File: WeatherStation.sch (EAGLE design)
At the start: 17 parts, among them J1 EDISON_CONNECTOR_FULLMOUNTING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, J2 EDISON_CONNECTOR_FULLHEADER, U1 MCP73831

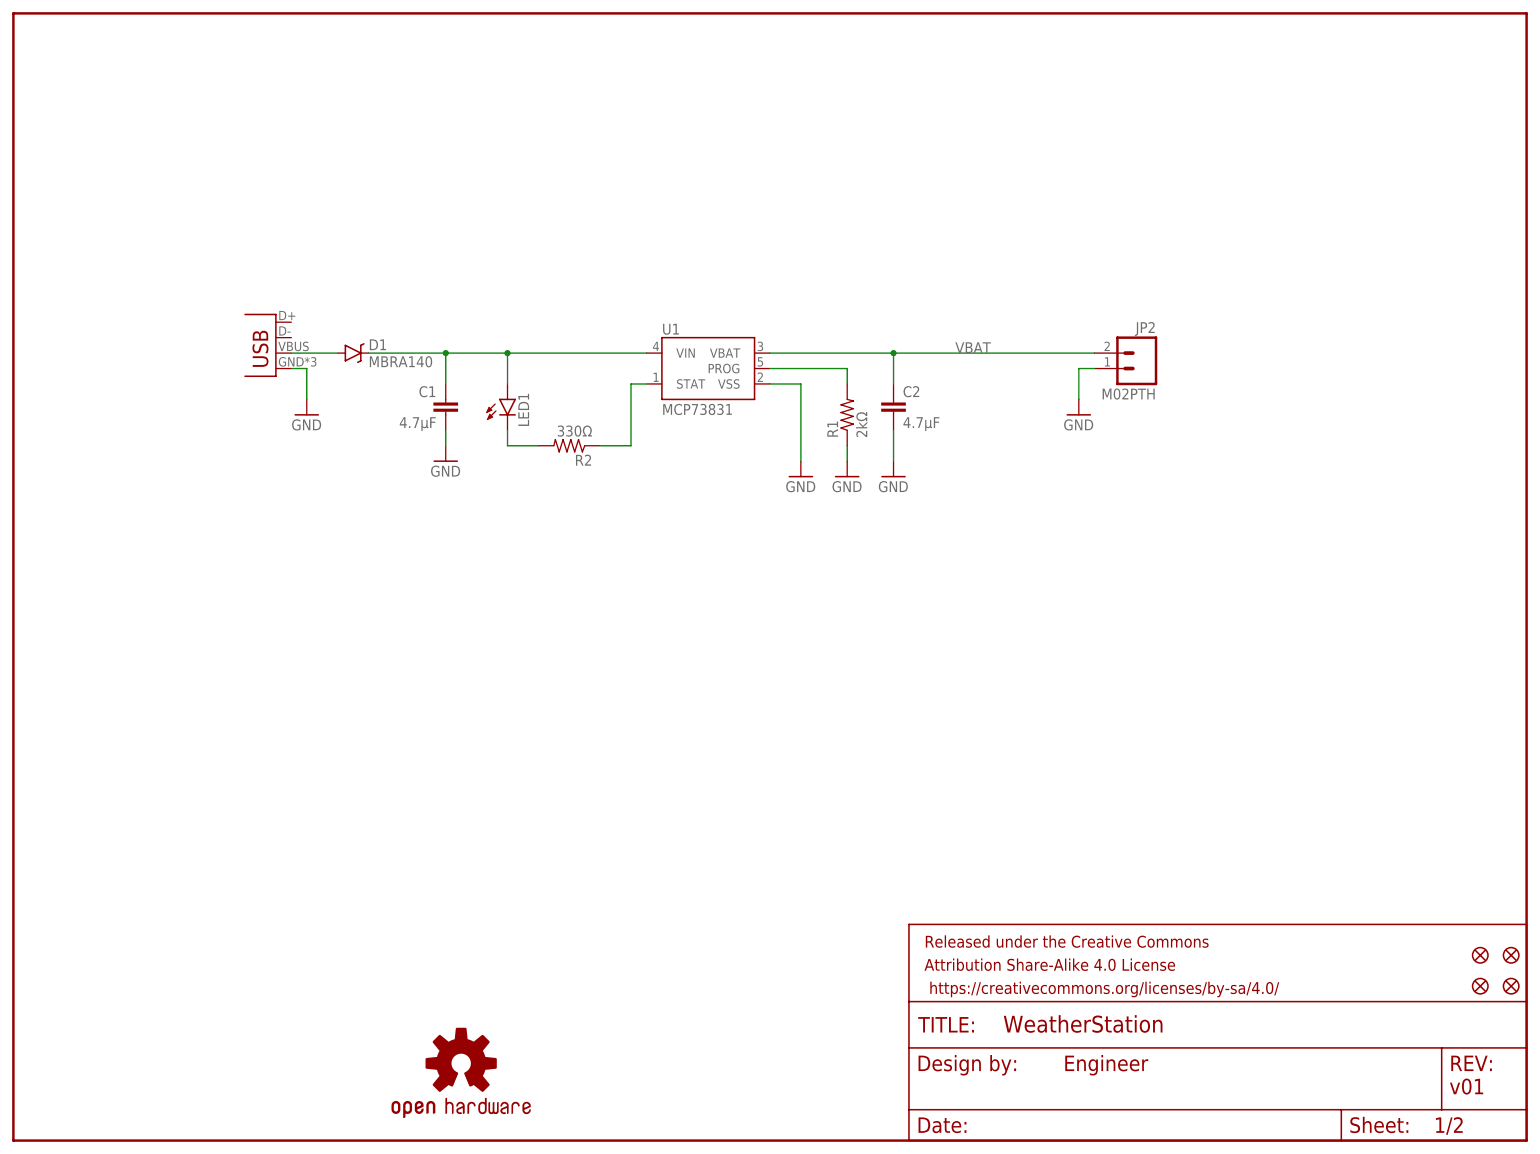
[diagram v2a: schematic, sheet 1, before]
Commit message: placed HTU21D, MPL3115A2, MIC5205-3.3V, PCA9306
RH/temp, barometric pressure/temp, LDO voltage regulator and 1.8-3.3V
logic level shifter.
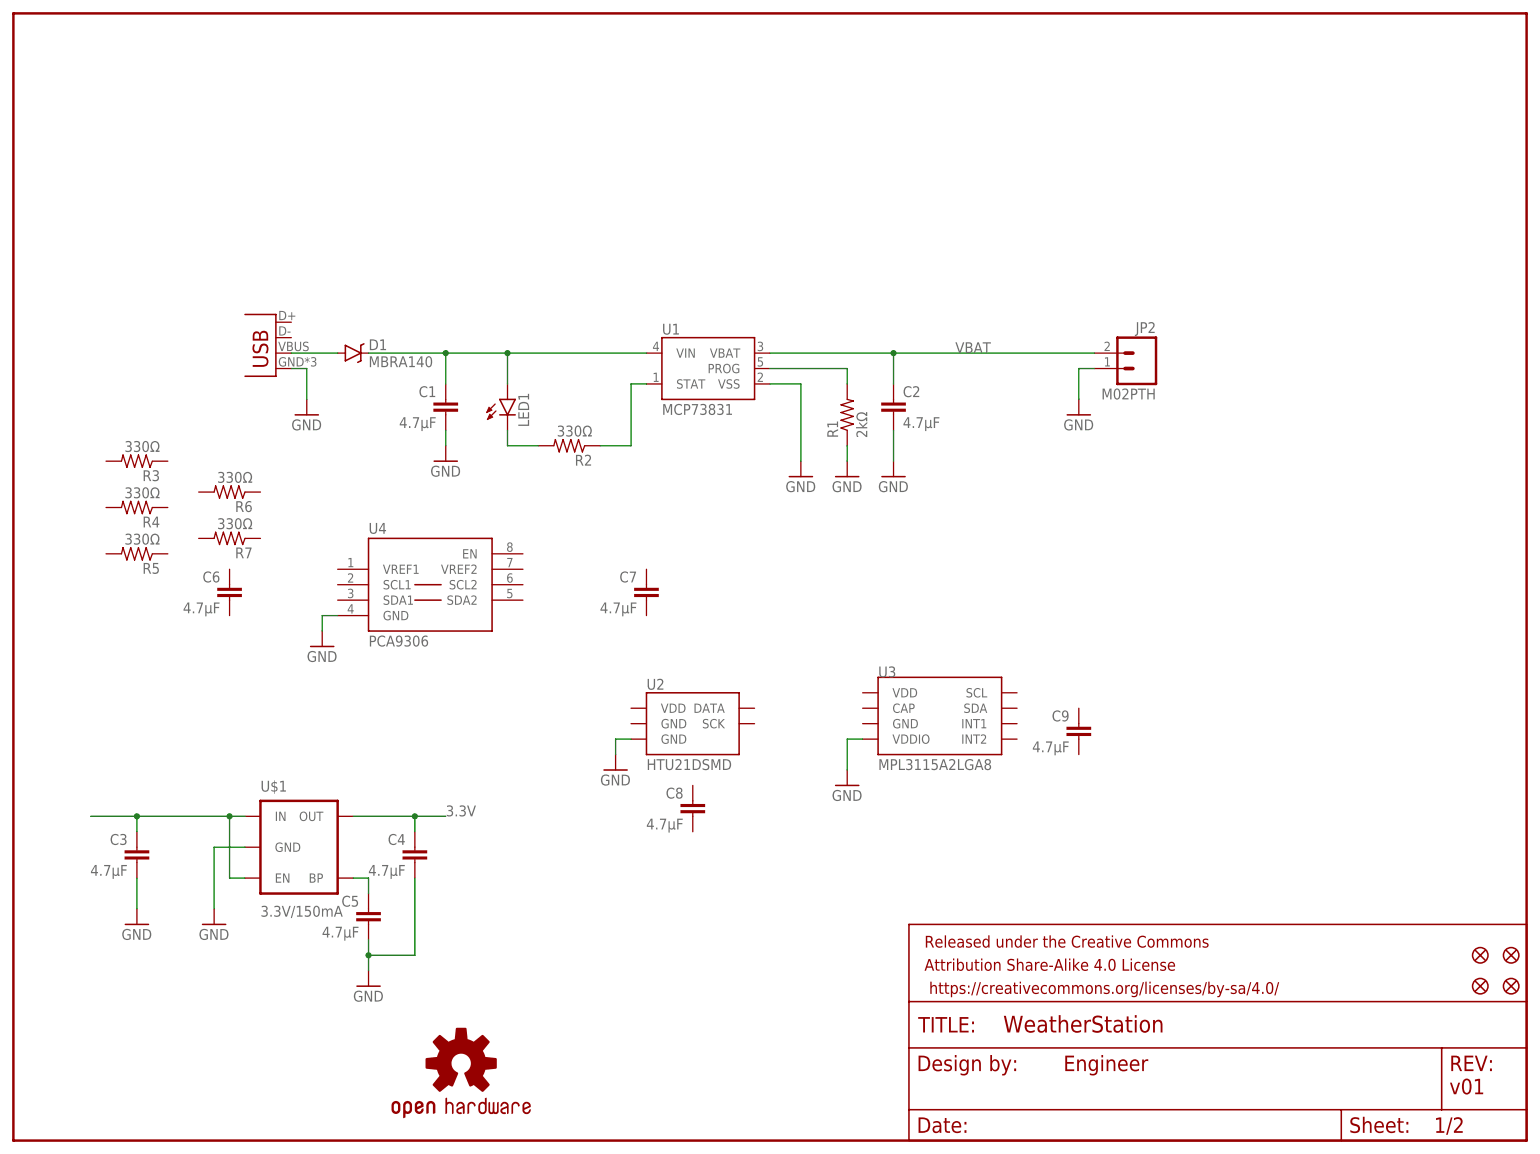
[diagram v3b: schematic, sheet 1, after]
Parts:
- added C3, C4, C5, C6, C7, C8, C9: 4.7µF, SparkFun-Capacitors:CAP0805
- added R3, R4, R5, R6, R7: 330Ω, SparkFun-Resistors:RESISTOR0603-RES
- added U$1: 3.3V/150mA, SparkFun-PowerIC:V_REG_MIC52053.3V
- added U2: HTU21DSMD, SparkFun-Sensors:HTU21DSMD
- added U3: MPL3115A2LGA8, SparkFun-Sensors:MPL3115A2LGA8
- added U4: PCA9306, SparkFun-DigitalIC:PCA9306
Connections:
- new net N$7: C3.1, U$1.EN, U$1.IN
- new net N$8: C5.1, U$1.BP
- net 3.3V: now also C4.1, U$1.OUT
- net GND: now also C3.2, C4.2, C5.2, U$1.GND, U2.GND@7, U3.VDDIO, U4.GND
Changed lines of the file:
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@@
 <part name="JP2" library="SparkFun-Connectors" deviceset="M02" device="PTH"/>
 <part name="GND8" library="SparkFun-Aesthetics" deviceset="GND" device=""/>
+<part name="U2" library="SparkFun-Sensors" deviceset="HTU21D" device="SMD"/>
+<part name="U3" library="SparkFun-Sensors" deviceset="MPL3115A2" device="LGA8"/>
+<part name="U4" library="SparkFun-DigitalIC" deviceset="PCA9306" device="" value="PCA9306"/>
+<part name="U$1" library="SparkFun-PowerIC" deviceset="V_REG_MIC5205" device="3.3V" value="3.3V/150mA"/>
+<part name="GND9" library="SparkFun-Aesthetics" deviceset="GND" device=""/>
+<part name="GND10" library="SparkFun-Aesthetics" deviceset="GND" device=""/>
+<part name="GND11" library="SparkFun-Aesthetics" deviceset="GND" device=""/>
+<part name="GND12" library="SparkFun-Aesthetics" deviceset="GND" device=""/>
+<part name="C3" library="SparkFun-Capacitors" deviceset="CAP" device="0805" value="4.7µF"/>
+<part name="C4" library="SparkFun-Capacitors" deviceset="CAP" device="0805" value="4.7µF"/>
+<part name="C5" library="SparkFun-Capacitors" deviceset="CAP" device="0805" value="4.7µF"/>
+<part name="GND13" library="SparkFun-Aesthetics" deviceset="GND" device=""/>
+<part name="GND14" library="SparkFun-Aesthetics" deviceset="GND" device=""/>
+<part name="C6" library="SparkFun-Capacitors" deviceset="CAP" device="0805" value="4.7µF"/>
+<part name="C7" library="SparkFun-Capacitors" deviceset="CAP" device="0805" value="4.7µF"/>
+<part name="R3" library="SparkFun-Resistors" deviceset="RESISTOR" device="0603-RES" value="330Ω"/>
+<part name="R4" library="SparkFun-Resistors" deviceset="RESISTOR" device="0603-RES" value="330Ω"/>
+<part name="R5" library="SparkFun-Resistors" deviceset="RESISTOR" device="0603-RES" value="330Ω"/>
+<part name="R6" library="SparkFun-Resistors" deviceset="RESISTOR" device="0603-RES" value="330Ω"/>
+<part name="R7" library="SparkFun-Resistors" deviceset="RESISTOR" device="0603-RES" value="330Ω"/>
+<part name="C8" library="SparkFun-Capacitors" deviceset="CAP" device="0805" value="4.7µF"/>
+<part name="C9" library="SparkFun-Capacitors" deviceset="CAP" device="0805" value="4.7µF"/>
 </parts>
 <sheets>
@@
 <instance part="JP2" gate="G$1" x="185.42" y="127" rot="MR0"/>
 <instance part="GND8" gate="1" x="175.26" y="119.38"/>
+<instance part="U2" gate="U$1" x="111.76" y="68.58"/>
+<instance part="U3" gate="G$1" x="152.4" y="71.12"/>
+<instance part="U4" gate="G$1" x="68.58" y="88.9"/>
+<instance part="U$1" gate="G$1" x="48.26" y="48.26"/>
+<instance part="GND9" gate="1" x="137.16" y="58.42"/>
+<instance part="GND10" gate="1" x="99.06" y="60.96"/>
+<instance part="GND11" gate="1" x="50.8" y="81.28"/>
+<instance part="GND12" gate="1" x="33.02" y="35.56"/>
+<instance part="C3" gate="G$1" x="20.32" y="45.72" rot="MR0"/>
+<instance part="C4" gate="G$1" x="66.04" y="45.72" rot="MR0"/>
+<instance part="C5" gate="G$1" x="58.42" y="35.56" rot="MR0"/>
+<instance part="GND13" gate="1" x="20.32" y="35.56"/>
+<instance part="GND14" gate="1" x="58.42" y="25.4"/>
+<instance part="C6" gate="G$1" x="35.56" y="88.9" rot="MR0"/>
+<instance part="C7" gate="G$1" x="104.14" y="88.9" rot="MR0"/>
+<instance part="R3" gate="G$1" x="20.32" y="111.76" rot="R180"/>
+<instance part="R4" gate="G$1" x="20.32" y="104.14" rot="R180"/>
+<instance part="R5" gate="G$1" x="20.32" y="96.52" rot="R180"/>
+<instance part="R6" gate="G$1" x="35.56" y="106.68" rot="R180"/>
+<instance part="R7" gate="G$1" x="35.56" y="99.06" rot="R180"/>
+<instance part="C8" gate="G$1" x="111.76" y="53.34" rot="MR0"/>
+<instance part="C9" gate="G$1" x="175.26" y="66.04" rot="MR0"/>
 </instances>
 <busses>
@@
 <wire x1="175.26" y1="127" x2="175.26" y2="121.92" width="0.1524" layer="91"/>
 </segment>
+<segment>
+<pinref part="GND11" gate="1" pin="GND"/>
+<pinref part="U4" gate="G$1" pin="GND"/>
+<wire x1="50.8" y1="83.82" x2="50.8" y2="86.36" width="0.1524" layer="91"/>
+<wire x1="50.8" y1="86.36" x2="53.34" y2="86.36" width="0.1524" layer="91"/>
+</segment>
+<segment>
+<pinref part="GND10" gate="1" pin="GND"/>
+<pinref part="U2" gate="U$1" pin="GND@7"/>
+<wire x1="99.06" y1="63.5" x2="99.06" y2="66.04" width="0.1524" layer="91"/>
+<wire x1="99.06" y1="66.04" x2="101.6" y2="66.04" width="0.1524" layer="91"/>
+</segment>
+<segment>
+<pinref part="GND9" gate="1" pin="GND"/>
+<pinref part="U3" gate="G$1" pin="VDDIO"/>
+<wire x1="137.16" y1="60.96" x2="137.16" y2="66.04" width="0.1524" layer="91"/>
+<wire x1="137.16" y1="66.04" x2="139.7" y2="66.04" width="0.1524" layer="91"/>
+</segment>
+<segment>
+<pinref part="U$1" gate="G$1" pin="GND"/>
+<pinref part="GND12" gate="1" pin="GND"/>
+<wire x1="38.1" y1="48.26" x2="33.02" y2="48.26" width="0.1524" layer="91"/>
+<wire x1="33.02" y1="48.26" x2="33.02" y2="38.1" width="0.1524" layer="91"/>
+</segment>
+<segment>
+<pinref part="C3" gate="G$1" pin="2"/>
+<pinref part="GND13" gate="1" pin="GND"/>
+<wire x1="20.32" y1="43.18" x2="20.32" y2="38.1" width="0.1524" layer="91"/>
+</segment>
+<segment>
+<pinref part="C4" gate="G$1" pin="2"/>
+<wire x1="66.04" y1="43.18" x2="66.04" y2="30.48" width="0.1524" layer="91"/>
+<wire x1="66.04" y1="30.48" x2="58.42" y2="30.48" width="0.1524" layer="91"/>
+<pinref part="GND14" gate="1" pin="GND"/>
+<wire x1="58.42" y1="30.48" x2="58.42" y2="27.94" width="0.1524" layer="91"/>
+<pinref part="C5" gate="G$1" pin="2"/>
+<wire x1="58.42" y1="33.02" x2="58.42" y2="30.48" width="0.1524" layer="91"/>
+<junction x="58.42" y="30.48"/>
+</segment>
 </net>
 <net name="VBAT" class="0">
@@
 </segment>
 </net>
+<net name="3.3V" class="0">
+<segment>
+<pinref part="U$1" gate="G$1" pin="OUT"/>
+<wire x1="55.88" y1="53.34" x2="66.04" y2="53.34" width="0.1524" layer="91"/>
+<pinref part="C4" gate="G$1" pin="1"/>
+<wire x1="66.04" y1="53.34" x2="71.12" y2="53.34" width="0.1524" layer="91"/>
+<wire x1="66.04" y1="53.34" x2="66.04" y2="50.8" width="0.1524" layer="91"/>
+<junction x="66.04" y="53.34"/>
+<label x="71.12" y="53.34" size="1.778" layer="95"/>
+</segment>
+</net>
+<net name="N$7" class="0">
+<segment>
+<pinref part="U$1" gate="G$1" pin="EN"/>
+<wire x1="38.1" y1="43.18" x2="35.56" y2="43.18" width="0.1524" layer="91"/>
+<wire x1="35.56" y1="43.18" x2="35.56" y2="53.34" width="0.1524" layer="91"/>
+<pinref part="U$1" gate="G$1" pin="IN"/>
+<wire x1="35.56" y1="53.34" x2="38.1" y2="53.34" width="0.1524" layer="91"/>
+<wire x1="12.7" y1="53.34" x2="20.32" y2="53.34" width="0.1524" layer="91"/>
+<junction x="35.56" y="53.34"/>
+<pinref part="C3" gate="G$1" pin="1"/>
+<wire x1="20.32" y1="53.34" x2="35.56" y2="53.34" width="0.1524" layer="91"/>
+<wire x1="20.32" y1="53.34" x2="20.32" y2="50.8" width="0.1524" layer="91"/>
+<junction x="20.32" y="53.34"/>
+</segment>
+</net>
+<net name="N$8" class="0">
+<segment>
+<pinref part="U$1" gate="G$1" pin="BP"/>
+<pinref part="C5" gate="G$1" pin="1"/>
+<wire x1="55.88" y1="43.18" x2="58.42" y2="43.18" width="0.1524" layer="91"/>
+<wire x1="58.42" y1="43.18" x2="58.42" y2="40.64" width="0.1524" layer="91"/>
+</segment>
+</net>

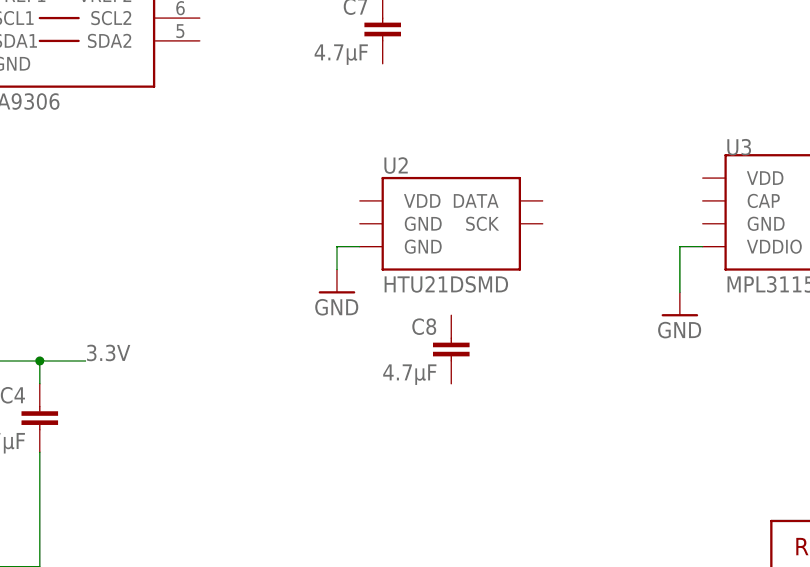
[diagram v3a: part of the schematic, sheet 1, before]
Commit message: connected schematic for HTU21D
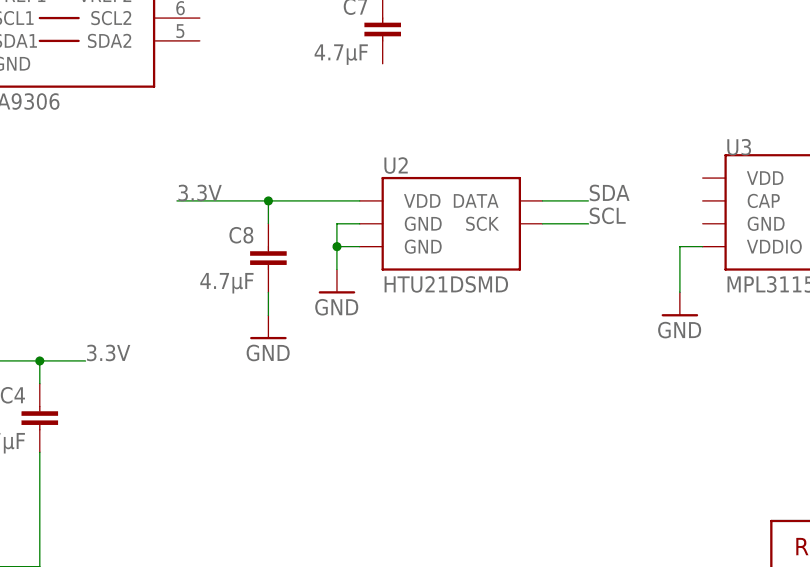
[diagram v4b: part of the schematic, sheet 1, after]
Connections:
- new net SCL: U2.SCK
- new net SDA: U2.DATA
- net 3.3V: now also C8.1, U2.VDD
- net GND: now also C8.2, U2.GND@2
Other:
- moved on the sheet: C8
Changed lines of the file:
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@@
 <part name="C8" library="SparkFun-Capacitors" deviceset="CAP" device="0805" value="4.7µF"/>
 <part name="C9" library="SparkFun-Capacitors" deviceset="CAP" device="0805" value="4.7µF"/>
+<part name="GND15" library="SparkFun-Aesthetics" deviceset="GND" device=""/>
 </parts>
 <sheets>
@@
 <instance part="R6" gate="G$1" x="35.56" y="106.68" rot="R180"/>
 <instance part="R7" gate="G$1" x="35.56" y="99.06" rot="R180"/>
-<instance part="C8" gate="G$1" x="111.76" y="53.34" rot="MR0"/>
+<instance part="C8" gate="G$1" x="91.44" y="63.5" rot="MR0"/>
 <instance part="C9" gate="G$1" x="175.26" y="66.04" rot="MR0"/>
+<instance part="GND15" gate="1" x="91.44" y="55.88"/>
 </instances>
 <busses>
@@
 <wire x1="99.06" y1="63.5" x2="99.06" y2="66.04" width="0.1524" layer="91"/>
 <wire x1="99.06" y1="66.04" x2="101.6" y2="66.04" width="0.1524" layer="91"/>
+<pinref part="U2" gate="U$1" pin="GND@2"/>
+<wire x1="101.6" y1="68.58" x2="99.06" y2="68.58" width="0.1524" layer="91"/>
+<wire x1="99.06" y1="68.58" x2="99.06" y2="66.04" width="0.1524" layer="91"/>
+<junction x="99.06" y="66.04"/>
 </segment>
 <segment>
@@
 <junction x="58.42" y="30.48"/>
 </segment>
+<segment>
+<pinref part="C8" gate="G$1" pin="2"/>
+<pinref part="GND15" gate="1" pin="GND"/>
+<wire x1="91.44" y1="60.96" x2="91.44" y2="58.42" width="0.1524" layer="91"/>
+</segment>
 </net>
 <net name="VBAT" class="0">
@@
 <junction x="66.04" y="53.34"/>
 <label x="71.12" y="53.34" size="1.778" layer="95"/>
+</segment>
+<segment>
+<pinref part="U2" gate="U$1" pin="VDD"/>
+<wire x1="81.28" y1="71.12" x2="91.44" y2="71.12" width="0.1524" layer="91"/>
+<pinref part="C8" gate="G$1" pin="1"/>
+<wire x1="91.44" y1="71.12" x2="101.6" y2="71.12" width="0.1524" layer="91"/>
+<wire x1="91.44" y1="71.12" x2="91.44" y2="68.58" width="0.1524" layer="91"/>
+<junction x="91.44" y="71.12"/>
+<label x="81.28" y="71.12" size="1.778" layer="95"/>
 </segment>
 </net>
@@
 </segment>
 </net>
+<net name="SDA" class="0">
+<segment>
+<pinref part="U2" gate="U$1" pin="DATA"/>
+<wire x1="127" y1="71.12" x2="121.92" y2="71.12" width="0.1524" layer="91"/>
+<label x="127" y="71.12" size="1.778" layer="95"/>
+</segment>
+</net>
+<net name="SCL" class="0">
+<segment>
+<pinref part="U2" gate="U$1" pin="SCK"/>
+<wire x1="127" y1="68.58" x2="121.92" y2="68.58" width="0.1524" layer="91"/>
+<label x="127" y="68.58" size="1.778" layer="95"/>
+</segment>
+</net>
